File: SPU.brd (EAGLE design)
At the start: 160 x 130 mm, 396 parts, among them Q2 CSTCR6M00G53Z

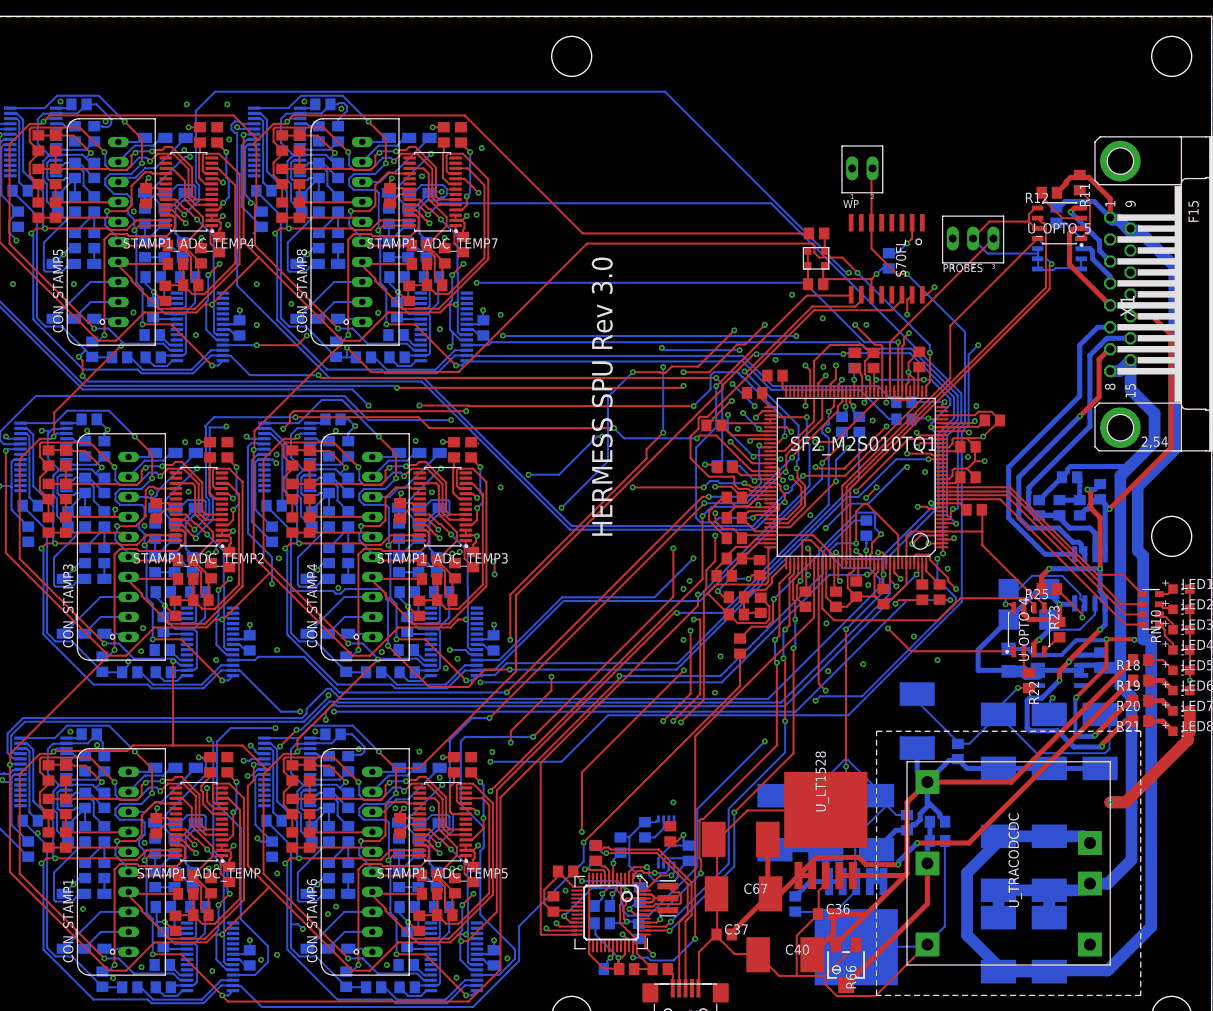
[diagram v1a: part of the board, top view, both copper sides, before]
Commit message: Improves labelling
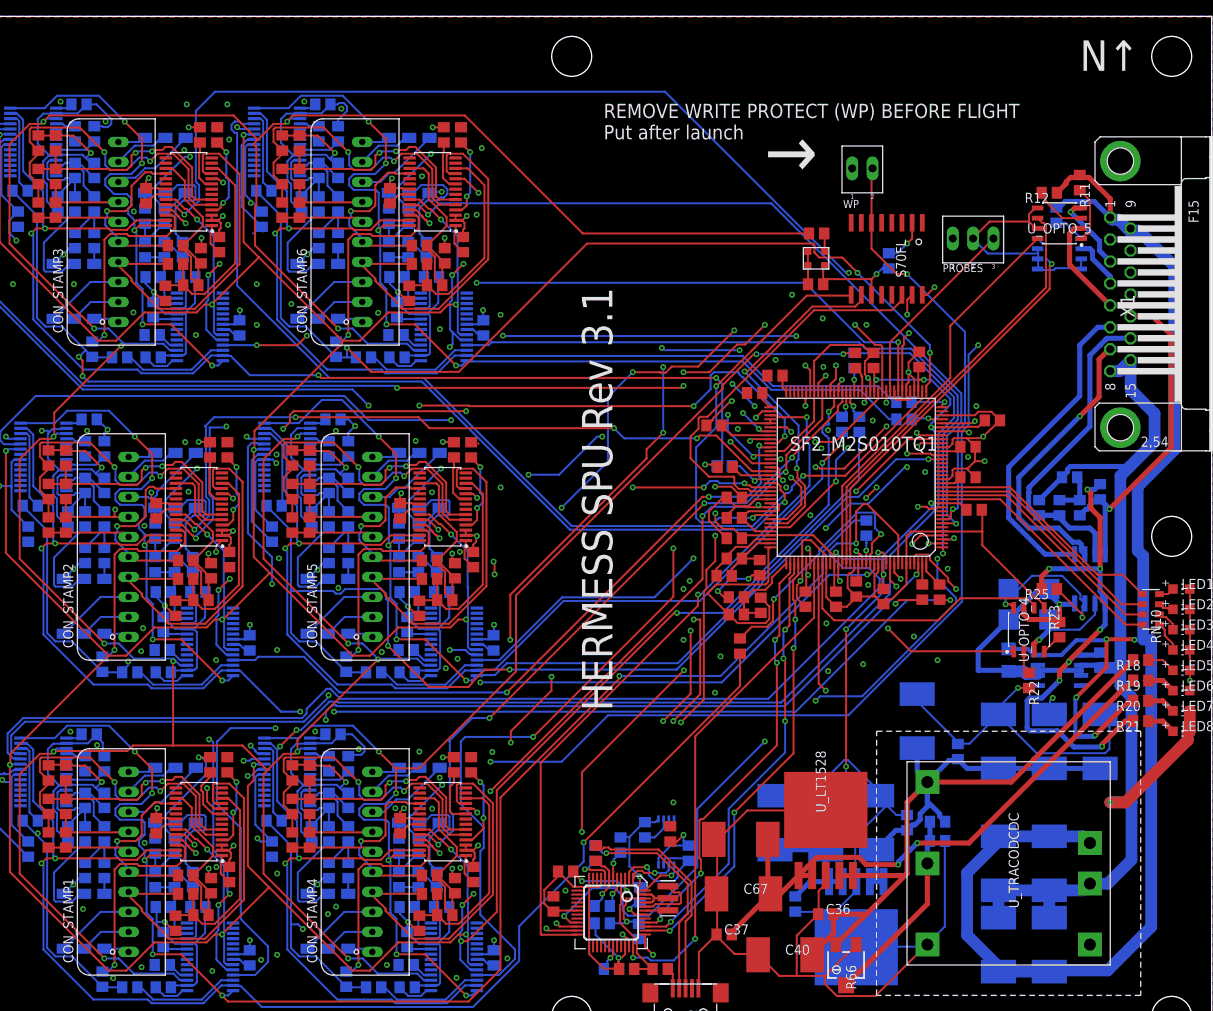
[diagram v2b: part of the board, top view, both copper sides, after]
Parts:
- removed CON_STAMP8: IL-AG5-10P-S3T2, con-jae:IL-AG5-10P-S3T2
- added CON_STAMP2: IL-AG5-10P-S3T2, con-jae:IL-AG5-10P-S3T2
- moved CON_STAMP6 78.8 mm to (58.4, 88.9)
- moved CON_STAMP5 50.6 mm to (59.7, 49.5)
- moved CON_STAMP3 39.4 mm to (27.9, 88.9)
- moved CON_STAMP4 39.4 mm to (59.7, 10.2)
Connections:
- net GND: now also CON_STAMP2.P$7; no longer CON_STAMP8.P$7
- net STAMP2_SG1_AIN1: now also CON_STAMP2.P$1; no longer CON_STAMP3.P$1
- net STAMP2_SG1_AIN2: now also CON_STAMP2.P$2; no longer CON_STAMP3.P$2
- net STAMP2_SG1_AIN3: now also CON_STAMP2.P$3; no longer CON_STAMP3.P$3
- net STAMP2_SG2_AIN1: now also CON_STAMP2.P$10; no longer CON_STAMP3.P$10
- net STAMP2_SG2_AIN2: now also CON_STAMP2.P$9; no longer CON_STAMP3.P$9
- net STAMP2_SG2_AIN3: now also CON_STAMP2.P$8; no longer CON_STAMP3.P$8
- net STAMP2_TEMP_AIN1: now also CON_STAMP2.P$4; no longer CON_STAMP3.P$4
- net STAMP2_TEMP_AIN2: now also CON_STAMP2.P$5; no longer CON_STAMP3.P$5
- net STAMP2_TEMP_AIN3: now also CON_STAMP2.P$6; no longer CON_STAMP3.P$6
- net STAMP3_SG1_AIN1: now also CON_STAMP3.P$1; no longer CON_STAMP5.P$1
- net STAMP3_SG1_AIN2: now also CON_STAMP3.P$2; no longer CON_STAMP5.P$2
- net STAMP3_SG1_AIN3: now also CON_STAMP3.P$3; no longer CON_STAMP5.P$3
- net STAMP3_SG2_AIN1: now also CON_STAMP3.P$10; no longer CON_STAMP5.P$10
- net STAMP3_SG2_AIN2: now also CON_STAMP3.P$9; no longer CON_STAMP5.P$9
- net STAMP3_SG2_AIN3: now also CON_STAMP3.P$8; no longer CON_STAMP5.P$8
- net STAMP3_TEMP_AIN1: now also CON_STAMP3.P$4; no longer CON_STAMP5.P$4
- net STAMP3_TEMP_AIN2: now also CON_STAMP3.P$5; no longer CON_STAMP5.P$5
- net STAMP3_TEMP_AIN3: now also CON_STAMP3.P$6; no longer CON_STAMP5.P$6
- net STAMP4_SG1_AIN1: now also CON_STAMP4.P$1; no longer CON_STAMP6.P$1
- net STAMP4_SG1_AIN2: now also CON_STAMP4.P$2; no longer CON_STAMP6.P$2
- net STAMP4_SG1_AIN3: now also CON_STAMP4.P$3; no longer CON_STAMP6.P$3
- net STAMP4_SG2_AIN1: now also CON_STAMP4.P$10; no longer CON_STAMP6.P$10
- net STAMP4_SG2_AIN2: now also CON_STAMP4.P$9; no longer CON_STAMP6.P$9
- net STAMP4_SG2_AIN3: now also CON_STAMP4.P$8; no longer CON_STAMP6.P$8
- net STAMP4_TEMP_AIN1: now also CON_STAMP4.P$4; no longer CON_STAMP6.P$4
- net STAMP4_TEMP_AIN2: now also CON_STAMP4.P$5; no longer CON_STAMP6.P$5
- net STAMP4_TEMP_AIN3: now also CON_STAMP4.P$6; no longer CON_STAMP6.P$6
- net STAMP5_SG1_AIN1: now also CON_STAMP5.P$1; no longer CON_STAMP4.P$1
- net STAMP5_SG1_AIN2: now also CON_STAMP5.P$2; no longer CON_STAMP4.P$2
- net STAMP5_SG1_AIN3: now also CON_STAMP5.P$3; no longer CON_STAMP4.P$3
- net STAMP5_SG2_AIN1: now also CON_STAMP5.P$10; no longer CON_STAMP4.P$10
- net STAMP5_SG2_AIN2: now also CON_STAMP5.P$9; no longer CON_STAMP4.P$9
- net STAMP5_SG2_AIN3: now also CON_STAMP5.P$8; no longer CON_STAMP4.P$8
- net STAMP5_TEMP_AIN1: now also CON_STAMP5.P$4; no longer CON_STAMP4.P$4
- net STAMP5_TEMP_AIN2: now also CON_STAMP5.P$5; no longer CON_STAMP4.P$5
- net STAMP5_TEMP_AIN3: now also CON_STAMP5.P$6; no longer CON_STAMP4.P$6
- net STAMP6_SG1_AIN1: now also CON_STAMP6.P$1; no longer CON_STAMP8.P$1
- net STAMP6_SG1_AIN2: now also CON_STAMP6.P$2; no longer CON_STAMP8.P$2
- net STAMP6_SG1_AIN3: now also CON_STAMP6.P$3; no longer CON_STAMP8.P$3
- net STAMP6_SG2_AIN1: now also CON_STAMP6.P$10; no longer CON_STAMP8.P$10
- net STAMP6_SG2_AIN2: now also CON_STAMP6.P$9; no longer CON_STAMP8.P$9
- net STAMP6_SG2_AIN3: now also CON_STAMP6.P$8; no longer CON_STAMP8.P$8
- net STAMP6_TEMP_AIN1: now also CON_STAMP6.P$4; no longer CON_STAMP8.P$4
- net STAMP6_TEMP_AIN2: now also CON_STAMP6.P$5; no longer CON_STAMP8.P$5
- net STAMP6_TEMP_AIN3: now also CON_STAMP6.P$6; no longer CON_STAMP8.P$6
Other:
- board text added: "HERMESS SPU Rev 3.1"
- board text added: "N↑"
- board text added: "REMOVE WRITE PROTECT (WP) BEFORE FLIGHT Put after launch"
- board text added: "→"
- board text removed: "HERMESS SPU Rev 3.0"

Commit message: Updates schematics
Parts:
- removed FTDI: FT2232D, smf2:FTDI2232D
- removed LED6, LED7, LED8: 1V9, adafruit:CHIP-LED0805
- removed R5: 4k7, rcl:R0805
- removed R6, R8: 27, rcl:R0805
- removed R64, R65: inf, rcl:R0805
- removed R66: inf, rcl:RTRIM3224X
- removed R7: 1k5, rcl:R0805
- removed RN10: 330, resistor-dil:EXBS8V
- removed U_LT1: LT1528, aSparkFun:Q5-DD
- added C71, C72, C73: 100n, rcl:C0805
- added C74, C75: 22p, rcl:C0805
- added L1, L2: (no value), rcl:L1812
- added Q1, Q3, Q4, Q5, Q6: BSS123, transistor-small-signal:SOT23
- added R34, R43, R44, R53, R57: 1k, rcl:R0805
- added R37, R38, R39, R42: 600, rcl:R0805
- added R47, R48: 330, rcl:R0805
- added R49, R52: 680, rcl:R0805
- added R54: 3R65, rcl:R0805
- added REF4V096: LM4030, selfmade:SOT-23
- added SF2_M2S010TQ2: SF2_M2S010TQ144, smf2:TQFP144
- added TPS78512QKVURQ1: TPS785, selfmade:TO-252-5
- added U$1, U$2, U$3: NXB0108PWJ, selfmade:TSSOP-20
- added USB: FT2232HL, smf2:LQFP64
- added ZE05H-4P-2V: ZE05-4P-2V, con-hirose:ZE05H-4P-2V
- C24, C26: value 100n -> 4u7
- C27: value 100n -> 150n
- C3, C5: value 4.7u -> 4u7
- C30, C31, C32: value 10u -> 100n; device rcl:E/7260-38W -> rcl:C0805
- Q2: value CSTCR6M00G53Z -> 12MHz; device murata-filter:CSTCR6M -> adafruit:HC49UP
- R19: value 330 -> 680
- R20: value 4k7 -> 680
- R21: value 470 -> 1k
- R22: value 2k -> 1k
- R4: value 10k -> 2
- R9: value 470 -> 12k
- X1: device con-subd:F15HP -> con-subd:M15H
- moved R1 696.9 mm to (-49.5, -594.4)
- moved C20 695.7 mm to (-55.9, -594.4)
- moved C19 693.8 mm to (-62.2, -594.4)
- moved C9 690.8 mm to (-49.5, -581.7), turned to 0 degrees
- moved C10 687.7 mm to (-43.2, -581.7), turned to 0 degrees
- moved C8 687.5 mm to (-55.9, -581.7)
- moved C16 681.6 mm to (-43.2, -588.0), turned to 0 degrees
- moved C7 677.9 mm to (-62.2, -581.7)
- moved C3 672.4 mm to (-44.5, -594.4)
- moved C15 672.2 mm to (-49.5, -588.0), turned to 0 degrees
- moved C14 671.2 mm to (-55.9, -588.0), turned to 0 degrees
- moved C13 670.4 mm to (-62.2, -588.0), turned to 0 degrees
- moved R2 669.8 mm to (-34.3, -594.4), turned to 0 degrees
- moved C11 665.8 mm to (-36.8, -581.7), turned to 0 degrees
- moved R3 664.6 mm to (-29.2, -594.4)
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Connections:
- removed net 5V-28V: C43.1, R16.1, R21.2, R25.2, U_7805.1, U_MAX488.1
- removed net HB_MSS: RN10.3, SF2_M2S010TQ1.14
- removed net HB_STAMPS: RN10.1, SF2_M2S010TQ1.16
- removed net HB_STORAGE: RN10.2, SF2_M2S010TQ1.15
- removed net LED4: RN10.4, SF2_M2S010TQ1.13
- removed net USB_N: CN1.D-, R8.2
- removed net USB_P: CN1.D+, R6.2
- removed net VCCINT: C10.1, C11.1, C12.1, C13.1, C14.1, C29.2, C31.+, C32.+, C7.1, C8.1, C9.1, SF2_M2S010TQ1.105, SF2_M2S010TQ1.12, SF2_M2S010TQ1.121, SF2_M2S010TQ1.133, SF2_M2S010TQ1.31, SF2_M2S010TQ1.39, SF2_M2S010TQ1.50, SF2_M2S010TQ1.95, U_LT1.1, U_LT1.2
- new net 1V2: C10.1, C11.1, C12.1, C13.1, C14.1, C29.1, C7.1, C8.1, C9.1, R37.1, R38.1, R39.1, R42.1, SF2_M2S010TQ2.105, SF2_M2S010TQ2.114, SF2_M2S010TQ2.12, SF2_M2S010TQ2.121, SF2_M2S010TQ2.127, SF2_M2S010TQ2.133, SF2_M2S010TQ2.138, SF2_M2S010TQ2.25, SF2_M2S010TQ2.31, SF2_M2S010TQ2.35, SF2_M2S010TQ2.39, SF2_M2S010TQ2.50, SF2_M2S010TQ2.95, TPS78512QKVURQ1.3, U$1.P10, U$1.P2, U$2.P10, U$2.P2, U$3.P10, U$3.P2
- new net 4V096: R105.2, R111.2, R124.2, R130.2, R143.2, R149.2, R181.2, R187.2, R33.2, R54.1, R74.2, R86.2, R92.2, REF4V096.P4, U$10.P$5, U$11.P$5, U$12.P$5, U$13.P$5, U$14.P$5, U$15.P$5, U$16.P$5, U$19.P$5, U$20.P$5, U$6.P$5, U$7.P$5, U$9.P$5
- new net 5V-NONISO: C43.1, R16.1, R25.2, U_7805.1, U_MAX488.1
- new net ACD_START_1V2: U$3.P8
- new net ADC_START_1V2: SF2_M2S010TQ1.128
- new net LED_FPGA_LOADED: Q3.1, R44.2, SF2_M2S010TQ1.23
- new net LED_HB_MEMSYNC: Q6.1, R53.2, SF2_M2S010TQ1.28
- new net LED_HB_MSS: Q5.1, R34.2, SF2_M2S010TQ1.24
- new net LED_RECORDING: Q4.1, R21.2, SF2_M2S010TQ1.27
- new net N$175: LED3.A, R49.2
- new net N$176: R47.2, ZE05H-4P-2V.P4
- new net N$177: LED3.C, Q4.3
- new net N$178: R48.2, ZE05H-4P-2V.P2
- new net N$179: C30.2, USB.12, USB.37, USB.49, USB.64
- new net N$180: C25.2, C26.2, L2.2, USB.9
- new net N$28: R35.2, U$1.P18
- new net N$36: SF2_M2S010TQ1.118, U$2.P3
- new net N$42: SF2_M2S010TQ1.122, U$2.P1
- new net N$44: Q1.3, U_OPTO_4.2
- new net N$53: SF2_M2S010TQ1.131, U$1.P4
- new net N$54: SF2_M2S010TQ1.134, U$1.P5
- new net N$57: SF2_M2S010TQ1.137, U$1.P8
- new net N$58: SF2_M2S010TQ1.141, U$1.P9
- new net N$59: SF2_M2S010TQ1.38, U$3.P6
- new net N$60: SF2_M2S010TQ1.110, U$2.P9
- new net N$61: SF2_M2S010TQ1.111, U$2.P8
- new net N$62: SF2_M2S010TQ1.112, U$2.P7
- new net N$63: SF2_M2S010TQ1.115, U$2.P6
- new net N$66: SF2_M2S010TQ1.116, U$2.P5
- new net N$67: SF2_M2S010TQ1.117, U$2.P4
- new net N$68: SF2_M2S010TQ1.30, U$3.P7
- new net N$71: R60.1, SF2_M2S010TQ1.1
- new net N$72: R61.1, SF2_M2S010TQ1.2
- new net N$73: R57.2, USB.14
- new net N$76: C27.1, R4.1, SF2_M2S010TQ2.69
- new net N$77: LED5.A, R52.2
- new net STAMP1_CS_TEMP_1V2: SF2_M2S010TQ1.142, U$3.P9
- net 28V: no longer R20.2
- net 28VGND: now also U_OPTO_4.5; no longer LED7.C, LED8.C
- net 3V3: now also C28.2, C31.2, C32.2, C71.2, C72.2, C73.2, L1.1, L2.1, R22.2, R4.2, R57.1, SF2_M2S010TQ2.104, SF2_M2S010TQ2.17, SF2_M2S010TQ2.41, SF2_M2S010TQ2.45, SF2_M2S010TQ2.54, SF2_M2S010TQ2.6, SF2_M2S010TQ2.62, SF2_M2S010TQ2.68, SF2_M2S010TQ2.77, SF2_M2S010TQ2.80, SF2_M2S010TQ2.86, SF2_M2S010TQ2.97, SF2_M2S010TQ2.99, TPS78512QKVURQ1.1, TPS78512QKVURQ1.2, U$1.P19, U$2.P19, U$3.P19, USB.20, USB.31, USB.42, USB.50, USB.56; no longer C24.2, C25.2, C26.2, C27.2, FTDI.14, FTDI.3, FTDI.31, FTDI.42, R105.2, R111.2, R124.2, R130.2, R143.2, R149.2, R181.2, R187.2, R19.2, R33.2, R74.2, R86.2, R9.1, R92.2, SF2_M2S010TQ1.104, SF2_M2S010TQ1.114, SF2_M2S010TQ1.127, SF2_M2S010TQ1.138, SF2_M2S010TQ1.17, SF2_M2S010TQ1.25, SF2_M2S010TQ1.35, SF2_M2S010TQ1.41, SF2_M2S010TQ1.45, SF2_M2S010TQ1.54, SF2_M2S010TQ1.6, SF2_M2S010TQ1.62, SF2_M2S010TQ1.76, SF2_M2S010TQ1.77, SF2_M2S010TQ1.80, SF2_M2S010TQ1.86, SF2_M2S010TQ1.97, SF2_M2S010TQ1.99, U$10.P$5, U$11.P$5, U$12.P$5, U$13.P$5, U$14.P$5, U$15.P$5, U$16.P$5, U$19.P$5, U$20.P$5, U$6.P$5, U$7.P$5, U$9.P$5
- net 5V: now also R18.1, R19.1, R20.1, R47.1, R48.1, R49.1, R52.1, R54.2; no longer C28.2, C30.+, R18.2, R65.1, R66.3, U_LT1.4, U_LT1.5
- net ADC_START: now also U$3.P13; no longer SF2_M2S010TQ1.128
- net DAPI_CTS: now also U$2.P14, USB.40; no longer FTDI.38, SF2_M2S010TQ1.112
- net DAPI_DSR: now also U$2.P16, USB.43; no longer FTDI.36, SF2_M2S010TQ1.116
- net DAPI_DTR: now also U$2.P17, USB.44; no longer FTDI.35, SF2_M2S010TQ1.117
- net DAPI_RTS: now also U$2.P15, USB.41; no longer FTDI.37, SF2_M2S010TQ1.115
- net DAPI_RXD: now also U$2.P12, USB.38; no longer FTDI.40, SF2_M2S010TQ1.110
- net DAPI_TXD: now also U$2.P13, USB.39; no longer FTDI.39, SF2_M2S010TQ1.111
- net EECLK: now also USB.62; no longer FTDI.1
- net EECS: now also USB.63; no longer FTDI.48
- net EED: now also USB.61; no longer FTDI.2
- net GND: now also C22.2, C24.2, C27.2, C29.2, C30.1, C31.1, C32.1, C71.1, C72.1, C73.1, C74.2, C75.2, Q1.2, Q3.2, Q4.2, Q5.2, Q6.2, R21.1, R34.1, R43.2, R44.1, R53.1, R9.1, REF4V096.P5, SF2_M2S010TQ2.11, SF2_M2S010TQ2.113, SF2_M2S010TQ2.119, SF2_M2S010TQ2.126, SF2_M2S010TQ2.132, SF2_M2S010TQ2.139, SF2_M2S010TQ2.18, SF2_M2S010TQ2.26, SF2_M2S010TQ2.34, SF2_M2S010TQ2.40, SF2_M2S010TQ2.42, SF2_M2S010TQ2.5, SF2_M2S010TQ2.51, SF2_M2S010TQ2.59, SF2_M2S010TQ2.65, SF2_M2S010TQ2.84, SF2_M2S010TQ2.96, SF2_M2S010TQ2.98, TPS78512QKVURQ1.4, TPS78512QKVURQ1.5, U$1.P11, U$2.P11, U$3.P11, USB.1, USB.10, USB.11, USB.13, USB.15, USB.25, USB.35, USB.47, USB.5, USB.51, ZE05H-4P-2V.P1, ZE05H-4P-2V.P3, ZE05H-4P-2V.P5, ZE05H-4P-2V.P6; no longer C22.1, C24.1, C27.1, C29.1, C30.-, C31.-, C32.-, FTDI.18, FTDI.25, FTDI.34, FTDI.45, FTDI.47, FTDI.9, LED2.C, LED3.C, LED4.C, LED5.C, LED6.C, Q2.2, R22.2, R4.1, R64.1, R66.1, SF2_M2S010TQ1.11, SF2_M2S010TQ1.113, SF2_M2S010TQ1.119, SF2_M2S010TQ1.126, SF2_M2S010TQ1.132, SF2_M2S010TQ1.139, SF2_M2S010TQ1.18, SF2_M2S010TQ1.26, SF2_M2S010TQ1.34, SF2_M2S010TQ1.40, SF2_M2S010TQ1.42, SF2_M2S010TQ1.5, SF2_M2S010TQ1.51, SF2_M2S010TQ1.59, SF2_M2S010TQ1.65, SF2_M2S010TQ1.84, SF2_M2S010TQ1.96, SF2_M2S010TQ1.98, U_LT1.3, U_LT1.6, U_OPTO_4.5
- net LO: now also R38.2, SF2_M2S010TQ1.125; no longer SF2_M2S010TQ1.123
- net N$11: now also C74.1, Q2.2, USB.2; no longer FTDI.8, R8.1
- net N$12: now also SF2_M2S010TQ1.32, U$3.P1; no longer FTDI.43, Q2.1
- net N$13: now also SF2_M2S010TQ1.33, U$3.P3; no longer C21.2, FTDI.6
- net N$14: now also SF2_M2S010TQ1.36, U$3.P4; no longer C22.2, FTDI.46, R9.2
- net N$15: now also C21.2, CN1.VBUS; no longer FTDI.4, R4.2, R5.1
- net N$16: now also C22.1, C24.1, L1.2, USB.4; no longer CN1.VBUS, R5.2
- net N$17: now also R36.2, U$1.P20; no longer R64.2, R65.2, R66.2, U_TRACODCDC.4
- net N$18: now also USB.16; no longer FTDI.24
- net N$19: now also USB.17; no longer FTDI.23
- net N$2: now also SF2_M2S010TQ2.72; no longer SF2_M2S010TQ1.72
- net N$20: now also USB.18; no longer FTDI.22
- net N$21: now also USB.19; no longer FTDI.21
- net N$22: now also SF2_M2S010TQ1.37, U$3.P5; no longer FTDI.44, Q2.3
- net N$27: now also U_OPTO_4.1; no longer U_OPTO_4.2
- net N$30: now also R18.2; no longer RN10.8
- net N$31: now also LED5.C, Q6.3; no longer LED2.A, RN10.7
- net N$32: now also LED4.C, Q5.3; no longer LED3.A, RN10.6
- net N$33: now also LED2.C, Q3.3; no longer LED4.A, RN10.5
- net N$4: now also SF2_M2S010TQ2.106; no longer SF2_M2S010TQ1.106
- net N$45: now also LED2.A, R19.2; no longer R35.2, SF2_M2S010TQ1.130
- net N$46: now also R40.1, U$2.P18; no longer R40.2, SF2_M2S010TQ1.143
- net N$47: now also U$1.P1; no longer R36.2
- net N$48: now also R41.1, U$2.P20; no longer R41.2, SF2_M2S010TQ1.144
- net N$5: now also SF2_M2S010TQ2.107; no longer SF2_M2S010TQ1.107
- net N$51: now also LED4.A, R20.2; no longer LED5.A, R18.1
- net N$52: now also SF2_M2S010TQ1.130, U$1.P3; no longer LED6.A, R19.1
- net N$55: now also SF2_M2S010TQ1.135, U$1.P6; no longer LED7.A, R20.1
- net N$56: now also SF2_M2S010TQ1.136, U$1.P7; no longer LED8.A, R21.1
- net N$6: now also SF2_M2S010TQ2.109; no longer SF2_M2S010TQ1.109
- net N$7: now also SF2_M2S010TQ2.108; no longer SF2_M2S010TQ1.108
- net N$74: now also R9.2, USB.6; no longer R60.2, SF2_M2S010TQ1.33
- net N$75: now also C75.1, Q2.1, USB.3; no longer R61.2, SF2_M2S010TQ1.36
- net N$8: now also CN1.D-, USB.7; no longer FTDI.5, R7.1
- net N$9: now also CN1.D+, USB.8; no longer FTDI.7, R6.1, R7.2
- net SODS: now also R37.2
- net SOE: now also R39.2, SF2_M2S010TQ1.123; no longer SF2_M2S010TQ1.125
- net STAMP1_CS_SG1: now also U$1.P13; no longer SF2_M2S010TQ1.137
- net STAMP1_CS_SG2: now also U$1.P12; no longer SF2_M2S010TQ1.141
- net STAMP1_CS_TEMP: now also U$3.P12; no longer SF2_M2S010TQ1.142
- net STAMP1_DRDY_SG1: now also U$1.P16; no longer SF2_M2S010TQ1.134
- net STAMP1_DRDY_SG2: now also U$1.P15; no longer SF2_M2S010TQ1.135
- net STAMP1_DRDY_TEMP: now also U$1.P14; no longer SF2_M2S010TQ1.136
- net STAMP1_MISO: now also U$1.P17; no longer SF2_M2S010TQ1.131
- net STAMP2_MOSI: now also R41.2; no longer R41.1
- net STAMP2_SCLK: now also R40.2; no longer R40.1
- net STAMP5_CS_SG1: now also U$3.P15; no longer SF2_M2S010TQ1.29
- net STAMP5_CS_SG2: now also SF2_M2S010TQ1.13; no longer SF2_M2S010TQ1.30
- net STAMP5_CS_TEMP: now also SF2_M2S010TQ1.14; no longer SF2_M2S010TQ1.32
- net STAMP5_DRDY_SG1: now also U$3.P18; no longer SF2_M2S010TQ1.24
- net STAMP5_DRDY_SG2: now also U$3.P17; no longer SF2_M2S010TQ1.27
- net STAMP5_DRDY_TEMP: now also U$3.P16; no longer SF2_M2S010TQ1.28
- net STAMP5_MISO: now also U$3.P20; no longer SF2_M2S010TQ1.23
- net STAMP6_CS_SG1: now also SF2_M2S010TQ1.9; no longer SF2_M2S010TQ1.3
- net STAMP6_CS_SG2: now also SF2_M2S010TQ1.10; no longer SF2_M2S010TQ1.4
- net STAMP6_CS_TEMP: now also SF2_M2S010TQ1.22; no longer SF2_M2S010TQ1.7
- net STAMP6_DRDY_SG1: now also SF2_M2S010TQ1.4; no longer SF2_M2S010TQ1.38
- net STAMP6_DRDY_SG2: now also SF2_M2S010TQ1.7; no longer SF2_M2S010TQ1.1
- net STAMP6_DRDY_TEMP: now also SF2_M2S010TQ1.8; no longer SF2_M2S010TQ1.2
- net STAMP6_MISO: now also SF2_M2S010TQ1.3; no longer SF2_M2S010TQ1.37
- net STAMP6_MOSI: now also R61.2; no longer R61.1
- net STAMP6_SCLK: now also R60.2; no longer R60.1
- net TM_RX: now also R42.2, SF2_M2S010TQ1.144; no longer SF2_M2S010TQ1.118
- net TM_TX: now also Q1.1, R43.1, SF2_M2S010TQ1.143; no longer SF2_M2S010TQ1.122, U_OPTO_4.1
- net WP: now also U$3.P14; no longer SF2_M2S010TQ1.8
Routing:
- net GND: track 1239.5 -> 905.0 mm, vias 85 -> 72
- net STAMP4_CS_SG1: track 156.4 -> 0.00 mm, vias 4 -> 0
- net VCCINT: track 153.6 -> 0.00 mm, vias 10 -> 0
- net STAMP3_CS_SG1: track 149.4 -> 0.00 mm, vias 5 -> 0
- net STAMP4_MISO: track 146.6 -> 2.51 mm, vias 7 -> 0
- net STAMP3_DRDY_SG1: track 131.9 -> 0.00 mm, vias 5 -> 0
- net STAMP3_MISO: track 133.2 -> 2.51 mm, vias 3 -> 0
- net STAMP5_CS_SG1: track 130.1 -> 0.00 mm, vias 2 -> 0
- net STAMP6_DRDY_SG1: track 129.5 -> 0.00 mm, vias 1 -> 0
- net STAMP5_MISO: track 131.2 -> 2.51 mm, vias 3 -> 0
- net STAMP3_CS_TEMP: track 127.3 -> 0.00 mm, vias 3 -> 0
- net 3V3: track 574.9 -> 455.8 mm, vias 98 -> 90
- net STAMP4_DRDY_SG1: track 116.4 -> 0.00 mm, vias 7 -> 0
- net STAMP4_DRDY_SG2: track 111.8 -> 0.00 mm, vias 3 -> 0
- net N$21: track 110.6 -> 0.00 mm, vias 6 -> 0
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
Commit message: Fixes LEDs
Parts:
- moved SF2_M2S010TQ1 255.9 mm to (66.7, -67.9)
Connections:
- removed net N$33: LED2.C, Q3.3
- new net N$181: LED2.C, Q3.3, ZE05H-4P-2V.P3
- net GND: no longer ZE05H-4P-2V.P1, ZE05H-4P-2V.P3
- net N$177: now also ZE05H-4P-2V.P1

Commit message: Finished Placement
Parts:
- removed C30, C32, C72: 100n, rcl:C0805
- removed R37, R38, R39: 600, rcl:R0805
- removed SF2_M2S010TQ2: SF2_M2S010TQ144, smf2:TQFP144
- added C76, C77, C78: 100n, rcl:C0805
- added C79: 4u7, rcl:C0805
- moved R3 704.9 mm to (76.8, 102.6), flipped to the bottom
- moved R2 704.4 mm to (80.0, 100.7), flipped to the bottom, turned to 270 degrees
- moved R4 703.4 mm to (72.0, 83.4), flipped to the bottom, turned to 90 degrees
- moved C3 702.4 mm to (82.1, 96.5), flipped to the bottom, turned to 90 degrees
- moved C5 702.3 mm to (76.8, 98.3), flipped to the bottom
- moved C19 701.1 mm to (77.5, 92.7), flipped to the bottom, turned to 270 degrees
- moved C13 699.7 mm to (70.8, 99.0), flipped to the bottom, turned to 180 degrees
- moved C20 698.2 mm to (56.1, 94.8), flipped to the bottom, turned to 90 degrees
- moved C14 697.8 mm to (66.8, 99.0), flipped to the bottom, turned to 180 degrees
- moved C27 696.8 mm to (69.9, 83.4), flipped to the bottom, turned to 90 degrees
- moved C7 694.1 mm to (73.8, 99.0), flipped to the bottom, turned to 90 degrees
- moved C8 689.7 mm to (72.6, 96.0), flipped to the bottom
- moved R1 684.5 mm to (74.8, 78.7), flipped to the bottom, turned to 90 degrees
- moved C16 684.3 mm to (57.1, 88.9), flipped to the bottom
- moved C9 683.8 mm to (74.7, 90.8), flipped to the bottom, turned to 90 degrees
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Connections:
- net N$8 renamed USB_N
- net N$9 renamed USB_P
- removed net ACD_START_1V2: U$3.P8
- removed net N$76: C27.1, R4.1, SF2_M2S010TQ2.69
- new net N$33: C27.1, R4.1, SF2_M2S010TQ1.69
- net 1V2: now also SF2_M2S010TQ1.105, SF2_M2S010TQ1.114, SF2_M2S010TQ1.12, SF2_M2S010TQ1.121, SF2_M2S010TQ1.127, SF2_M2S010TQ1.133, SF2_M2S010TQ1.138, SF2_M2S010TQ1.25, SF2_M2S010TQ1.31, SF2_M2S010TQ1.35, SF2_M2S010TQ1.39, SF2_M2S010TQ1.50, SF2_M2S010TQ1.95; no longer R37.1, R38.1, R39.1, SF2_M2S010TQ2.105, SF2_M2S010TQ2.114, SF2_M2S010TQ2.12, SF2_M2S010TQ2.121, SF2_M2S010TQ2.127, SF2_M2S010TQ2.133, SF2_M2S010TQ2.138, SF2_M2S010TQ2.25, SF2_M2S010TQ2.31, SF2_M2S010TQ2.35, SF2_M2S010TQ2.39, SF2_M2S010TQ2.50, SF2_M2S010TQ2.95
- net 3V3: now also SF2_M2S010TQ1.104, SF2_M2S010TQ1.17, SF2_M2S010TQ1.41, SF2_M2S010TQ1.45, SF2_M2S010TQ1.54, SF2_M2S010TQ1.6, SF2_M2S010TQ1.62, SF2_M2S010TQ1.68, SF2_M2S010TQ1.77, SF2_M2S010TQ1.80, SF2_M2S010TQ1.86, SF2_M2S010TQ1.97, SF2_M2S010TQ1.99; no longer C32.2, C72.2, SF2_M2S010TQ2.104, SF2_M2S010TQ2.17, SF2_M2S010TQ2.41, SF2_M2S010TQ2.45, SF2_M2S010TQ2.54, SF2_M2S010TQ2.6, SF2_M2S010TQ2.62, SF2_M2S010TQ2.68, SF2_M2S010TQ2.77, SF2_M2S010TQ2.80, SF2_M2S010TQ2.86, SF2_M2S010TQ2.97, SF2_M2S010TQ2.99
- net ADC_START_1V2: now also U$3.P8
- net GND: now also C76.1, C77.1, C78.1, C79.1, SF2_M2S010TQ1.11, SF2_M2S010TQ1.113, SF2_M2S010TQ1.119, SF2_M2S010TQ1.126, SF2_M2S010TQ1.132, SF2_M2S010TQ1.139, SF2_M2S010TQ1.18, SF2_M2S010TQ1.26, SF2_M2S010TQ1.34, SF2_M2S010TQ1.40, SF2_M2S010TQ1.42, SF2_M2S010TQ1.5, SF2_M2S010TQ1.51, SF2_M2S010TQ1.59, SF2_M2S010TQ1.65, SF2_M2S010TQ1.84, SF2_M2S010TQ1.96, SF2_M2S010TQ1.98; no longer C30.1, C32.1, C72.1, SF2_M2S010TQ2.11, SF2_M2S010TQ2.113, SF2_M2S010TQ2.119, SF2_M2S010TQ2.126, SF2_M2S010TQ2.132, SF2_M2S010TQ2.139, SF2_M2S010TQ2.18, SF2_M2S010TQ2.26, SF2_M2S010TQ2.34, SF2_M2S010TQ2.40, SF2_M2S010TQ2.42, SF2_M2S010TQ2.5, SF2_M2S010TQ2.51, SF2_M2S010TQ2.59, SF2_M2S010TQ2.65, SF2_M2S010TQ2.84, SF2_M2S010TQ2.96, SF2_M2S010TQ2.98
- net LO: no longer R38.2
- net N$179: now also C76.2, C77.2, C78.2, C79.2; no longer C30.2
- net N$2: now also SF2_M2S010TQ1.72; no longer SF2_M2S010TQ2.72
- net N$4: now also SF2_M2S010TQ1.106; no longer SF2_M2S010TQ2.106
- net N$5: now also SF2_M2S010TQ1.107; no longer SF2_M2S010TQ2.107
- net N$6: now also SF2_M2S010TQ1.109; no longer SF2_M2S010TQ2.109
- net N$7: now also SF2_M2S010TQ1.108; no longer SF2_M2S010TQ2.108
- net SODS: no longer R37.2
- net SOE: no longer R39.2
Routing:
- net ADC_START: track 538.6 -> 0.00 mm, vias 21 -> 0
- net SG_CLK: track 418.5 -> 0.00 mm, vias 15 -> 0
- net STAMP4_MOSI: track 200.0 -> 0.00 mm, vias 4 -> 0
- net STAMP1_SCLK: track 187.0 -> 0.00 mm, vias 6 -> 0
- net STAMP2_SCLK: track 160.7 -> 0.00 mm, vias 6 -> 0
- net 3V3: track 455.8 -> 297.1 mm, vias 90 -> 33
- net STAMP4_SCLK: track 151.0 -> 0.00 mm, vias 7 -> 0
- net STAMP1_CS_SG1: track 149.7 -> 0.00 mm, vias 1 -> 0
- net STAMP1_MISO: track 148.7 -> 2.51 mm, vias 3 -> 0
- net STAMP1_CS_SG2: track 142.2 -> 0.00 mm, vias 5 -> 0
- net STAMP3_SCLK: track 134.5 -> 0.00 mm, vias 6 -> 0
- net STAMP1_DRDY_SG2: track 133.8 -> 0.00 mm, vias 2 -> 0
- net STAMP1_DRDY_TEMP: track 130.9 -> 0.00 mm, vias 2 -> 0
- net STAMP1_DRDY_SG1: track 123.3 -> 0.00 mm, vias 2 -> 0
- net STAMP6_CS_SG1: track 125.2 -> 2.22 mm, vias 2 -> 1
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
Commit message: After AR 97.8%
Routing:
- net ADC_START: track 0.00 -> 585.1 mm, vias 0 -> 17
- net SG_CLK: track 0.00 -> 419.0 mm, vias 0 -> 13
- net 4V096: track 25.6 -> 423.9 mm, vias 0 -> 11
- net GND: track 920.8 -> 1223.5 mm, vias 80 -> 88
- net 1V2: track 43.3 -> 278.4 mm, vias 8 -> 13
- net TM_TX: track 2.71 -> 123.4 mm, vias 0 -> 2
- net 5V: track 111.2 -> 228.7 mm, vias 0 -> 1
- net WP: track 0.00 -> 116.0 mm, vias 0 -> 3
- net SOE: track 0.00 -> 115.3 mm, vias 0 -> 3
- net STAMP3_SCLK: track 0.00 -> 115.1 mm, vias 0 -> 3
- net LO: track 0.00 -> 113.6 mm, vias 0 -> 2
- net STAMP4_SCLK: track 0.00 -> 107.6 mm, vias 0 -> 5
- net STAMP4_MOSI: track 0.00 -> 102.5 mm, vias 0 -> 5
- net DAPI_DTR: track 0.00 -> 102.0 mm, vias 0 -> 4
- net DAPI_RXD: track 0.00 -> 97.7 mm, vias 0 -> 2
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
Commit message: During work commit
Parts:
- removed CN1: (no value), adafruit:USB-MINIB
- added USB_CONN: (no value), adafruit:USB-MINIB
- moved C75 111.3 mm to (141.4, 116.8), flipped to the top
- moved Q2 109.4 mm to (138.8, 108.6), flipped to the top, turned to 270 degrees
- moved C78 108.1 mm to (133.6, 103.5), flipped to the top, turned to 90 degrees
- moved C74 105.7 mm to (142.6, 102.6), flipped to the top, turned to 270 degrees
- moved C23 101.8 mm to (126.1, 114.5)
- moved USB 101.8 mm to (128.1, 110.6), turned to 180 degrees
- moved C77 101.1 mm to (127.5, 117.6)
- moved C73 101.1 mm to (130.3, 113.7)
- moved C76 101.1 mm to (132.6, 105.0)
- moved R57 101.1 mm to (131.5, 109.3)
- moved R27 100.7 mm to (120.6, 104.4), turned to 270 degrees
- moved R24 99.1 mm to (122.8, 100.5), turned to 90 degrees
- moved FT_EEPROM 95.5 mm to (127.7, 100.8), turned to 0 degrees
- moved C31 95.5 mm to (127.0, 104.4)
- moved C71 95.5 mm to (124.3, 111.3)
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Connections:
- net GND: now also USB_CONN.GND; no longer CN1.GND
- net N$15: now also USB_CONN.VBUS; no longer CN1.VBUS
- net USB_N: now also USB_CONN.D-; no longer CN1.D-
- net USB_P: now also USB_CONN.D+; no longer CN1.D+
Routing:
- net GND: track 1223.5 -> 0.00 mm, vias 88 -> 0
- net ADC_START: track 585.1 -> 0.00 mm, vias 17 -> 0
- net 4V096: track 423.9 -> 1.98 mm, vias 11 -> 0
- net 3V3: track 301.3 -> 6.26 mm, vias 33 -> 0
- net 1V2: track 278.4 -> 53.3 mm, vias 13 -> 4
- net 5V: track 228.7 -> 4.14 mm, vias 1 -> 0
- net 28VGND: track 198.7 -> 3.11 mm, vias 1 -> 0
- net 28V: track 150.7 -> 0.00 mm, vias 3 -> 0
- net STAMP5_MOSI: track 129.8 -> 0.00 mm, vias 3 -> 0
- net STAMP3_MOSI: track 128.9 -> 0.00 mm, vias 4 -> 0
- net STAMP2_MOSI: track 124.8 -> 0.00 mm, vias 4 -> 0
- net TM_TX: track 123.4 -> 0.00 mm, vias 2 -> 0
- net STAMP5_SCLK: track 123.4 -> 0.00 mm, vias 7 -> 0
- net STAMP6_MOSI: track 121.7 -> 0.00 mm, vias 3 -> 0
- net SOE: track 115.3 -> 0.00 mm, vias 3 -> 0
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- added copper zone on layer 1, net GND
- added copper zone on layer 15, net GND
- added copper zone on layer 16, net GND
- removed copper zone on layer 1, net 3V3
- removed copper zone on layer 16, net 3V3
